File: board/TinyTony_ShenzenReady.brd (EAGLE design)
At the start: 39 x 35.5 mm, 7 parts, among them U1 ATTINY85

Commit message: board
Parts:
- ISP1: value AVRISP-6 -> AVRISPPOGO; device adafruit:AVRISP -> tinytony_shenzenReady:AVRISP-50MIL
- moved ISP1 11.0 mm to (14.5, 13.8)
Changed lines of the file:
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@@
 </autorouter>
 <elements>
-<element name="ISP1" library="adafruit" package="AVRISP" value="AVRISP-6" x="25.4" y="12.7" smashed="yes" rot="R180">
-<attribute name="NAME" x="22.987" y="16.764" size="1.27" layer="25"/>
+<element name="ISP1" library="tinytony_shenzenReady" package="AVRISP-50MIL" value="AVRISPPOGO" x="14.478" y="13.843" smashed="yes" rot="R180">
+<attribute name="NAME" x="17.272" y="12.319" size="0.8128" layer="25" rot="R90"/>
 </element>
 <element name="JP1" library="tinytony_shenzenReady" package="1X02_ROUND" value="power" x="20.32" y="20.32"/>
@@
 <wire x1="15.97" y1="25.4" x2="19.05" y2="20.32" width="0" layer="19" extent="1-1"/>
 <wire x1="18.9484" y1="14.605" x2="19.05" y2="20.32" width="0" layer="19" extent="1-1"/>
-<wire x1="24.13" y1="10.16" x2="18.9484" y2="14.605" width="0" layer="19" extent="1-1"/>
-<wire x1="24.13" y1="6.35" x2="24.13" y2="10.16" width="0" layer="19" extent="1-1"/>
+<wire x1="14.478" y1="11.303" x2="18.9484" y2="14.605" width="0" layer="19" extent="1-1"/>
+<wire x1="24.13" y1="6.35" x2="14.478" y2="11.303" width="0" layer="19" extent="1-1"/>
 <wire x1="17.78" y1="6.35" x2="18.9484" y2="14.605" width="0" layer="19" extent="1-1"/>
 </signal>
@@
 <contactref element="JP1" pad="2"/>
 <wire x1="23.4" y1="25.4" x2="21.59" y2="20.32" width="0" layer="19" extent="1-1"/>
-<wire x1="24.13" y1="15.24" x2="21.59" y2="20.32" width="0" layer="19" extent="1-1"/>
-<wire x1="11.5316" y1="10.795" x2="24.13" y2="15.24" width="0" layer="19" extent="1-1"/>
+<wire x1="14.478" y1="13.843" x2="21.59" y2="20.32" width="0" layer="19" extent="1-1"/>
+<wire x1="11.5316" y1="10.795" x2="14.478" y2="13.843" width="0" layer="19" extent="1-1"/>
 <wire x1="15.24" y1="6.35" x2="11.5316" y2="10.795" width="0" layer="19" extent="1-1"/>
 </signal>
@@
 <contactref element="ISP1" pad="4"/>
 <contactref element="JP2" pad="1"/>
-<wire x1="18.9484" y1="10.795" x2="24.13" y2="12.7" width="0" layer="19" extent="1-1"/>
+<wire x1="18.9484" y1="10.795" x2="14.478" y2="12.573" width="0" layer="19" extent="1-1"/>
 <wire x1="21.59" y1="6.35" x2="18.9484" y2="10.795" width="0" layer="19" extent="1-1"/>
 </signal>
@@
 <contactref element="U1" pad="6"/>
 <contactref element="ISP1" pad="1"/>
-<wire x1="18.9484" y1="12.065" x2="26.67" y2="10.16" width="0" layer="19" extent="1-1"/>
+<wire x1="18.9484" y1="12.065" x2="15.748" y2="11.303" width="0" layer="19" extent="1-1"/>
 </signal>
 <signal name="7">
@@
 <contactref element="U1" pad="1"/>
 <contactref element="ISP1" pad="5"/>
-<wire x1="11.5316" y1="14.605" x2="26.67" y2="15.24" width="0" layer="19" extent="1-1"/>
+<wire x1="11.5316" y1="14.605" x2="15.748" y2="13.843" width="0" layer="19" extent="1-1"/>
 </signal>
 <signal name="2">
@@
 <contactref element="ISP1" pad="3"/>
 <contactref element="U$1" pad="1"/>
-<wire x1="11.5316" y1="12.065" x2="26.67" y2="12.7" width="0" layer="19" extent="1-1"/>
+<wire x1="11.5316" y1="12.065" x2="15.748" y2="12.573" width="0" layer="19" extent="1-1"/>
 <wire x1="12.7" y1="6.35" x2="11.5316" y2="12.065" width="0" layer="19" extent="1-1"/>
 </signal>

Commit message: yet another layout
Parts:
- moved R1 24.2 mm to (3.94, 14.2), turned to 180 degrees
- moved ISP1 13.5 mm to (5.71, 3.56), turned to 270 degrees
- moved JP1 13.1 mm to (13.5, 9.14), turned to 270 degrees
- moved R2 11.4 mm to (11.6, 14.2)
- moved JP2 10.2 mm to (13.3, 2.79), turned to 270 degrees
- moved U$1 9.45 mm to (7.11, 1.52)
- moved U1 9.14 mm to (7.11, 8.51)
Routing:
- net GND: track 0.00 -> 27.0 mm, vias 0 -> 2
- net VCC: track 0.00 -> 24.5 mm, vias 0 -> 1
- net 3: track 0.00 -> 12.4 mm, vias 0 -> 1
- net 5: track 0.00 -> 9.75 mm, vias 0 -> 1
- net 1: track 0.00 -> 8.80 mm
- net 6: track 0.00 -> 4.87 mm
- net 2: track 16.8 -> 14.6 mm
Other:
- board size 39 x 35.5 mm -> 15.5 x 16.6 mm

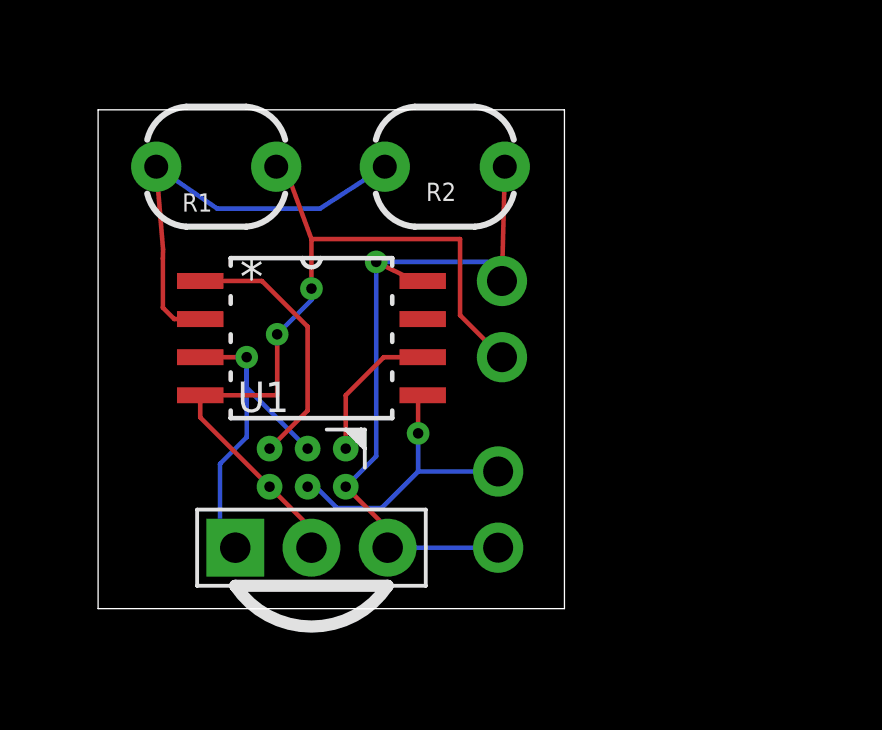
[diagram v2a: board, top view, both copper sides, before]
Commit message: 2 drivers and cap
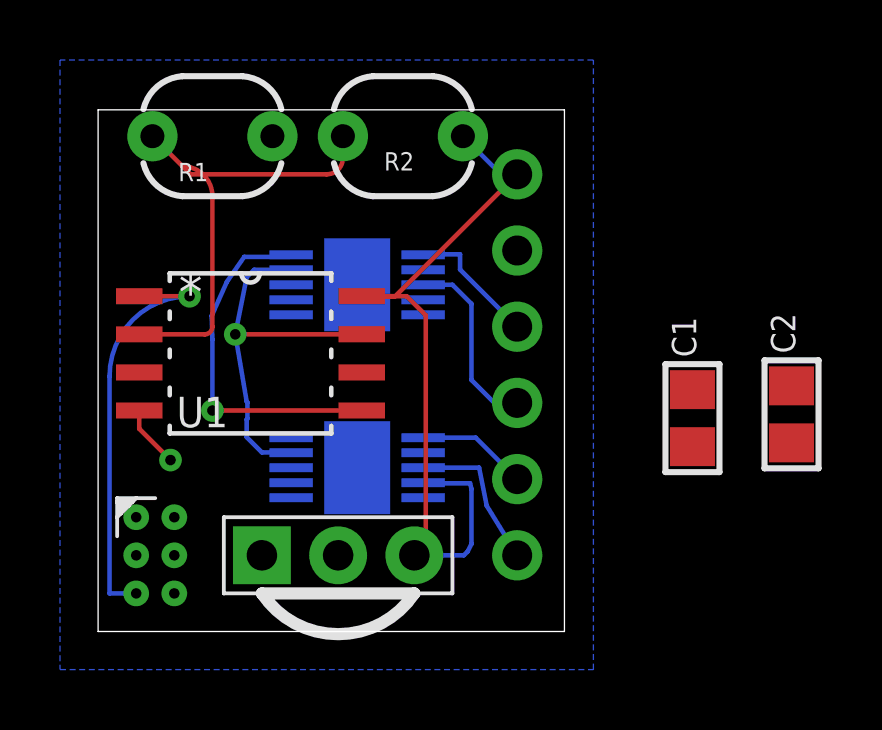
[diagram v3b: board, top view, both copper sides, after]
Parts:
- added C1, C2: (no value), microbuilder:0805_NOTHERMALS
- added JP3: MOTOR2, tinytony_shenzenReady:1X02_ROUND
- added U$2, U$3: DRV8830, tinytony_shenzenReady:DRV8830
- JP2: value motor driver -> MOTOR1
- moved ISP1 4.77 mm to (2.54, 0.00), turned to 0 degrees
- moved JP1 3.59 mm to (14.0, 12.7)
- moved U1 2.09 mm to (5.08, 8.00)
- moved R2 1.73 mm to (10.2, 15.2)
- moved R1 1.02 mm to (3.81, 15.2)
- moved U$1 0.92 mm to (8.00, 1.27)
- moved JP2 0.68 mm to (14.0, 2.54), turned to 90 degrees
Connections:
- new net N$1: U$3.P$8
- new net N$2: JP3.1, U$3.P$3
- new net N$3: JP2.1, U$2.P$3
- new net N$4: JP2.2, U$2.P$1
- new net N$5: JP3.2, U$3.P$1
- new net N$8: U$2.P$7
- net 5: now also U$2.P$10, U$3.P$10; no longer JP2.1
- net 7: now also U$2.P$9, U$3.P$9
- net GND: now also C1.1, C2.1, U$2.P$5, U$2.P$8, U$3.P$5, U$3.P$7
- net VCC: now also C1.2, C2.2, U$2.P$4, U$3.P$4; no longer JP2.2
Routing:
- net GND: track 27.0 -> 2.08 mm, vias 2 -> 1
- net 7: track 0.00 -> 12.9 mm, vias 0 -> 1
- net 3: track 12.4 -> 0.00 mm, vias 1 -> 0
- net N$2: track 0.00 -> 6.25 mm
- net N$3: track 0.00 -> 5.10 mm
- net 6: track 4.87 -> 0.00 mm
- net 1: track 8.80 -> 13.6 mm, vias 0 -> 1
- net N$5: track 0.00 -> 4.44 mm
- net N$4: track 0.00 -> 3.71 mm
- net 5: track 9.75 -> 12.0 mm
- net 2: track 14.6 -> 16.1 mm
- net VCC: track 24.5 -> 25.5 mm, vias 1 -> 0
- added copper zone on layer 16, net GND
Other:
- board size 15.5 x 16.6 mm -> 15.5 x 17.4 mm

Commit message: bigger, 1206cp
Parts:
- removed R1, R2: PHOTOCELLPTH, SparkFun-Sensors:PHOTOCELL
- added PHOTOCELL01, PHOTOCELL02: PHOTOCELL0N1, TinyTony_ShenzenReady:TO46-VT200
- C1, C2: device microbuilder:0805_NOTHERMALS -> TinyTony_ShenzenReady:1206
- moved JP2 23.9 mm to (3.81, 24.1), turned to 0 degrees
- moved C1 21.6 mm to (4.32, 21.0), turned to 180 degrees
- moved C2 18.3 mm to (12.2, 20.7), turned to 180 degrees
- moved JP3 16.7 mm to (11.4, 24.1), turned to 0 degrees
- moved U$2 12.4 mm to (4.42, 15.8), flipped to the top, turned to 270 degrees
- moved ISP1 7.03 mm to (7.24, 5.23), turned to 270 degrees
- moved U$3 6.57 mm to (12.3, 15.7), flipped to the top, turned to 270 degrees
- moved U1 4.02 mm to (8.89, 9.27)
- moved JP1 2.84 mm to (15.2, 10.2), turned to 90 degrees
- moved U$1 1.27 mm to (8.00, 2.54)
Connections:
- net 2: now also PHOTOCELL01.1, PHOTOCELL02.2; no longer R1.2, R2.1
- net GND: now also PHOTOCELL01.2; no longer R1.1
- net VCC: now also PHOTOCELL02.1; no longer R2.2
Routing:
- net VCC: track 25.5 -> 57.1 mm, vias 0 -> 3
- net 5: track 12.0 -> 25.6 mm, vias 1 -> 3
- net 3: track 0.00 -> 12.5 mm, vias 0 -> 1
- net 1: track 13.6 -> 5.99 mm
- net 6: track 0.00 -> 4.21 mm
- net N$4: track 3.71 -> 6.66 mm
- net 7: track 12.9 -> 15.4 mm, vias 1 -> 0
- net N$5: track 4.44 -> 6.61 mm
- net GND: track 2.08 -> 0.00 mm, vias 1 -> 8
- net N$3: track 5.10 -> 6.88 mm
- net 2: track 16.1 -> 15.2 mm
- net N$2: track 6.25 -> 7.07 mm
- added copper zone on layer 1, net GND
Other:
- board size 15.5 x 17.4 mm -> 16.5 x 25.4 mm
